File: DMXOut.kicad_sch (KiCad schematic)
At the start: 3 parts, among them J101 SJ2-25504B-SMT-TR, U101 LTC2863

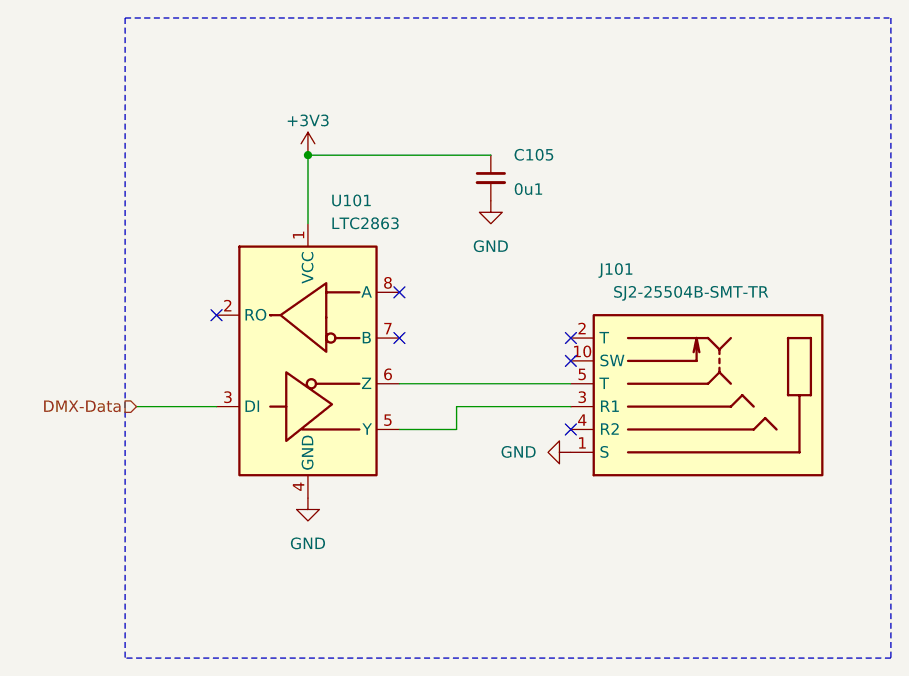
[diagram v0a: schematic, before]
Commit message: Update to Kicad 8
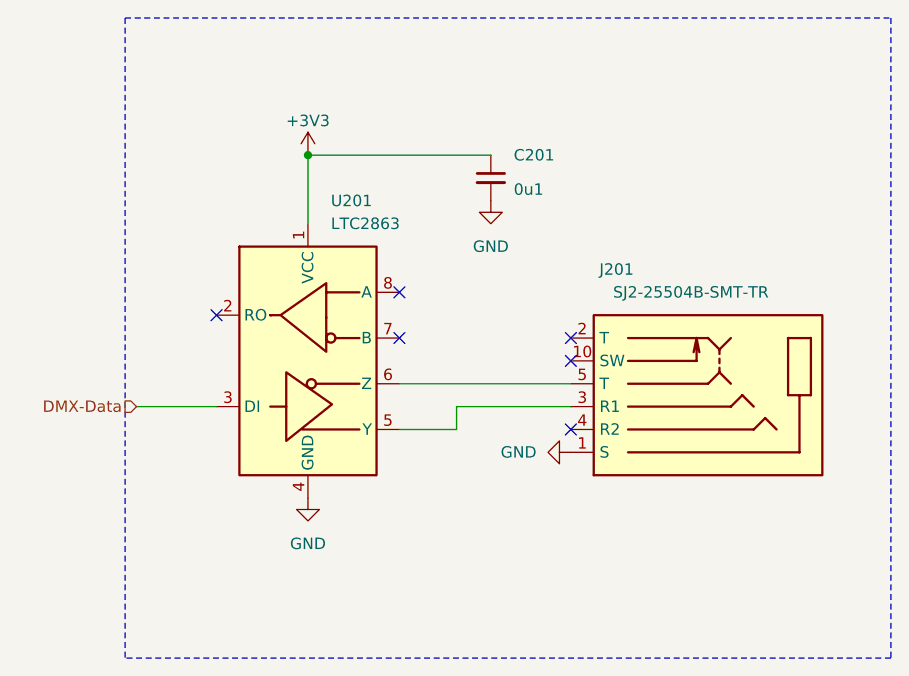
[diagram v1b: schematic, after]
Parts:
- renumbered C105 to C201, J101 to J201, U101 to U201

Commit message: Update TRS socket
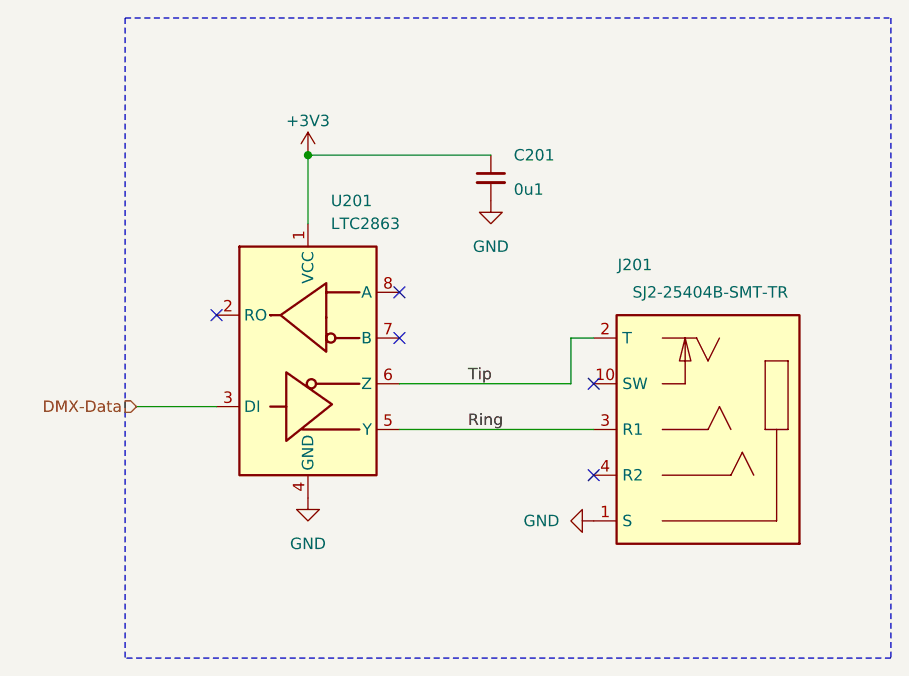
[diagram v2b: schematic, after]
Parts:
- J201: value SJ2-25504B-SMT-TR -> SJ2-25404B-SMT-TR; footprint V2_Connector_Audio:CUI_SJ2-25504B-SMT-TR -> V2_Connector_Audio:CUI_SJ2-25404B-SMT-TR; symbol V2_Connector_Audio:SJ2-25504B-SMT-TR -> V2_Connector_Audio:SJ2-25404B-SMT-TR
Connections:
- net Ring: now reaches J201.3 (R1), U201.5 (Y)
- net Tip: now reaches U201.6 (Z)
- net Tip: now also J201.2 (T); no longer J201.5 (T)
- no-connect marks 6 -> 5
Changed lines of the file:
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@@
 	(title_block
 		(title "DMX Out")
-		(date "2023-01-12")
+		(date "2024-07-17")
+		(rev "2")
 		(company "Versio Duo")
 	)
@@
 	)
 	(no_connect
-		(at 160.02 107.95)
+		(at 140.97 100.33)
 	)
 	(no_connect
-		(at 140.97 100.33)
+		(at 162.56 120.65)
 	)
 	(no_connect
-		(at 160.02 115.57)
-	)
-	(no_connect
-		(at 160.02 105.41)
+		(at 162.56 110.49)
 	)
 	(no_connect
@@
 	(wire
 		(pts
-			(xy 140.97 115.57) (xy 147.32 115.57)
-		)
-		(stroke
-			(width 0)
-			(type default)
-		)
-	)
-	(wire
-		(pts
 			(xy 140.97 110.49) (xy 160.02 110.49)
 		)
@@
 		)
 	)
+	(wire
+		(pts
+			(xy 160.02 105.41) (xy 160.02 110.49)
+		)
+		(stroke
+			(width 0)
+			(type default)
+		)
+	)
 	(polyline
 		(pts
@@
 	(wire
 		(pts
-			(xy 147.32 115.57) (xy 147.32 113.03)
-		)
-		(stroke
-			(width 0)
-			(type default)
-		)
-	)
-	(wire
-		(pts
 			(xy 130.81 85.09) (xy 130.81 92.71)
 		)
@@
 	(wire
 		(pts
-			(xy 147.32 113.03) (xy 160.02 113.03)
+			(xy 162.56 105.41) (xy 160.02 105.41)
+		)
+		(stroke
+			(width 0)
+			(type default)
+		)
+	)
+	(wire
+		(pts
+			(xy 140.97 115.57) (xy 162.56 115.57)
 		)
 		(stroke
@@
 			(width 0)
 			(type default)
+		)
+	)
+	(label "Ring"
+		(at 148.59 115.57 0)
+		(fields_autoplaced yes)
+		(effects
+			(font
+				(size 1.27 1.27)
+			)
+			(justify left bottom)
+		)
+	)
+	(label "Tip"
+		(at 148.59 110.49 0)
+		(fields_autoplaced yes)
+		(effects
+			(font
+				(size 1.27 1.27)
+			)
+			(justify left bottom)
 		)
 	)
@@
 	(symbol
 		(lib_id "power:GND")
-		(at 160.02 118.11 270)
+		(at 162.56 125.73 270)
 		(unit 1)
 		(exclude_from_sim no)
@@
 		(fields_autoplaced yes)
 		(property "Reference" "#PWR0204"
-			(at 153.67 118.11 0)
+			(at 156.21 125.73 0)
 			(effects
 				(font
@@
 		)
 		(property "Value" "GND"
-			(at 156.21 118.1099 90)
+			(at 158.75 125.7299 90)
 			(effects
 				(font
@@
 		)
 		(property "Footprint" ""
-			(at 160.02 118.11 0)
+			(at 162.56 125.73 0)
 			(effects
 				(font
@@
 		)
 		(property "Datasheet" ""
-			(at 160.02 118.11 0)
+			(at 162.56 125.73 0)
 			(effects
 				(font
@@
 		)
 		(property "Description" ""
-			(at 160.02 118.11 0)
+			(at 162.56 125.73 0)
 			(effects
 				(font
@@
 	)
 	(symbol
-		(lib_id "V2_Connector_Audio:SJ2-25504B-SMT-TR")
-		(at 175.26 111.76 0)
-		(mirror x)
+		(lib_id "V2_Connector_Audio:SJ2-25404B-SMT-TR")
+		(at 175.26 115.57 180)
 		(unit 1)
-		(exclude_from_sim yes)
+		(exclude_from_sim no)
 		(in_bom yes)
 		(on_board yes)
 		(dnp no)
 		(property "Reference" "J201"
-			(at 165.1 97.79 0)
-			(effects
-				(font
-					(size 1.27 1.27)
-				)
-			)
-		)
-		(property "Value" "SJ2-25504B-SMT-TR"
-			(at 173.355 100.33 0)
-			(effects
-				(font
-					(size 1.27 1.27)
-				)
-			)
-		)
-		(property "Footprint" "V2_Connector_Audio:CUI_SJ2-25504B-SMT-TR"
-			(at 162.56 97.79 0)
+			(at 167.132 97.282 0)
+			(effects
+				(font
+					(size 1.27 1.27)
+				)
+			)
+		)
+		(property "Value" "SJ2-25404B-SMT-TR"
+			(at 175.514 100.33 0)
+			(effects
+				(font
+					(size 1.27 1.27)
+				)
+			)
+		)
+		(property "Footprint" "V2_Connector_Audio:CUI_SJ2-25404B-SMT-TR"
+			(at 187.452 94.996 0)
 			(effects
 				(font
@@
 		)
 		(property "Datasheet" ""
-			(at 175.26 111.76 0)
+			(at 175.26 115.57 0)
 			(effects
 				(font
@@
 		)
 		(property "Description" ""
-			(at 175.26 111.76 0)
-			(effects
-				(font
-					(size 1.27 1.27)
-				)
+			(at 183.388 92.456 0)
+			(effects
+				(font
+					(size 1.27 1.27)
+				)
+				(justify left bottom)
 				(hide yes)
 			)
@@
 		(pin "4"
 		)
-		(pin "5"
-		)
 		(instances
